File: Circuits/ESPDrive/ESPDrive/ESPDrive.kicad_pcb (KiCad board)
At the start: 4 copper layers, 44 x 64 mm, 55 parts, among them Q1 AOSS32334C, U1 AP63203WU, U2 AP63201WU, U3 LTV-827S

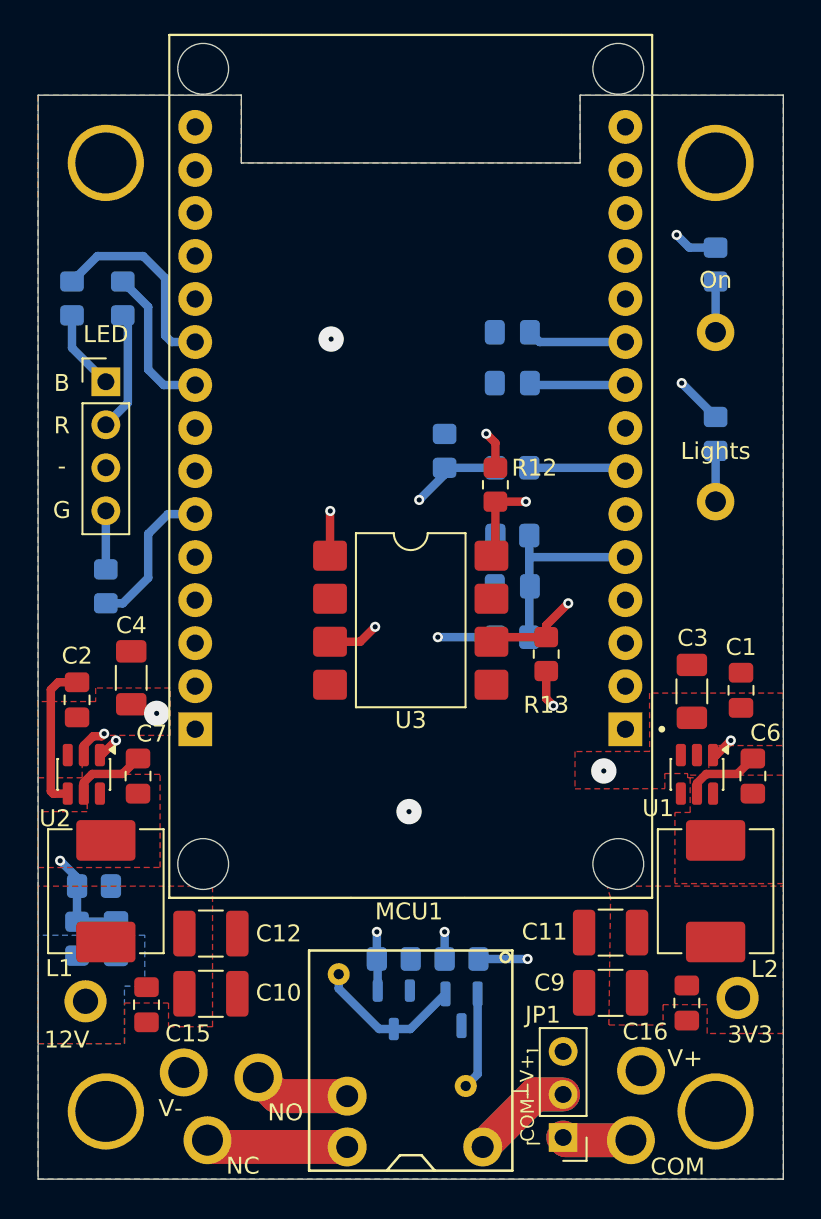
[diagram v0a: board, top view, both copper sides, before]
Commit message: ESPDrive: fixed regulator pad errors, small tweaks
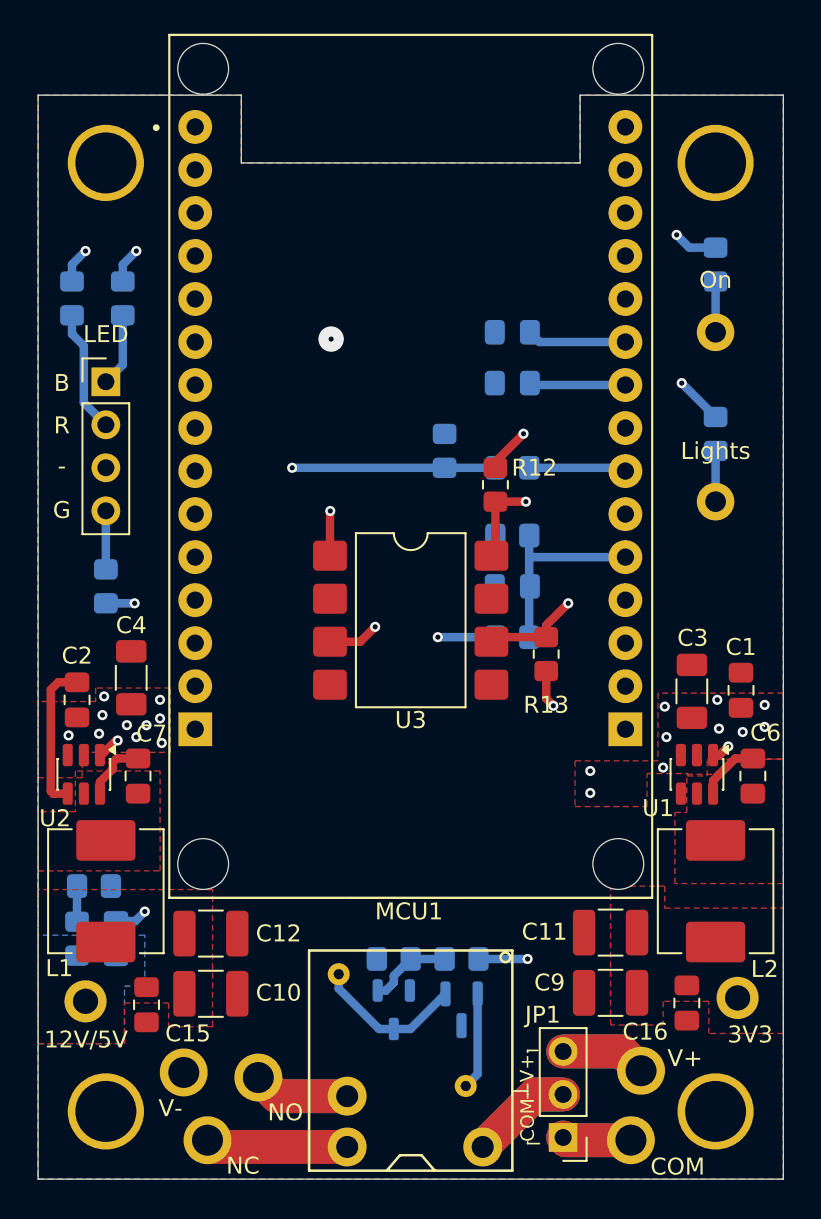
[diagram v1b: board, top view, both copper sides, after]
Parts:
- moved R14 3.00 mm to (132.0, 88.0)
- moved R16 3.00 mm to (135.0, 88.0)
- turned R4 to 180 degrees
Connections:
- C6 pad 1: Net-(U1-SW) -> Net-(U1-BST)
- C6 pad 2: Net-(U1-BST) -> Net-(U1-SW)
- C7 pad 1: Net-(U2-SW) -> Net-(U2-BST)
- C7 pad 2: Net-(U2-BST) -> Net-(U2-SW)
- L1 pad 1: Net-(U2-BST) -> Net-(U2-SW)
- L2 pad 1: Net-(U1-BST) -> Net-(U1-SW)
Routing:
- net +BATT: track 9.13 -> 29.4 mm, vias 5 -> 21
- net +3V3: track 72.5 -> 85.4 mm
- net Net-(U1-SW): track 4.52 -> 0.00 mm
- net Net-(U2-SW): track 4.45 -> 0.00 mm
- net Net-(Q1-G): track 9.08 -> 4.96 mm, vias 2 -> 0
- net C_r: track 8.98 -> 12.7 mm, vias 0 -> 1
- net Net-(U2-BST): track 0.00 -> 3.75 mm
- net Net-(U1-BST): track 0.00 -> 3.65 mm
- net C_b: track 12.0 -> 8.94 mm, vias 0 -> 1
- net Net-(U2-EN): track 38.7 -> 41.6 mm
- net Net-(U2-FB): track 16.1 -> 18.7 mm
- net C_g: track 8.98 -> 9.62 mm, vias 0 -> 1
- added copper zone on In1.Cu, net GNDREF
- added copper zone on F.Cu, net Net-(U1-SW)
- added copper zone on F.Cu, net Net-(U2-SW)
- removed copper zone on In1.Cu, net +BATT
- removed copper zone on F.Cu, net Net-(U1-BST)
- removed copper zone on F.Cu, net Net-(U2-BST)
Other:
- board text added: "12V/5V"
- board text removed: "12V"
